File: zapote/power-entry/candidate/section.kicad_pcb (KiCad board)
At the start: 2 copper layers, 230 x 190 mm, 53 parts, among them U1 GBU2510A, U10 C3D20065D, U11 UCC28180D, U12 10mohm, U13 10ohm, U14 10kohm, U15 1kohm, U16 100kohm, U17 91ohm, U18 220ohm, U19 16.2kohm, U2 0031.2510, U20 200kohm, U21 200kohm, U22 200kohm, U23 200kohm, U24 200kohm, U25 13kohm, U26 40.2kohm, U27 1uF, U28 2.7nF, U29 4.7uF, U3 B82726S2163N030, U30 220nF, U31 1nF, U32 680pF, U33 AO3400A, U34 SS14, U35 BAT54H,115, U36 560uF, U37 560uF, U38 560uF, U39 560uF, U4 SL32 10015, U40 1nF, U41 1714984, U42 61300211121, U43 61300211121, U44 61300211121, U45 AO3400A, U46 AO3400A, U47 100kohm, U48 100kohm, U49 1kohm, U5 RT33K012, U50 100kohm, U51 1714971, U52 150kohm, U53 150kohm, U6 0.22uF, U7 V150LA10AP, U8 760800301, U9 STW65N65DM2

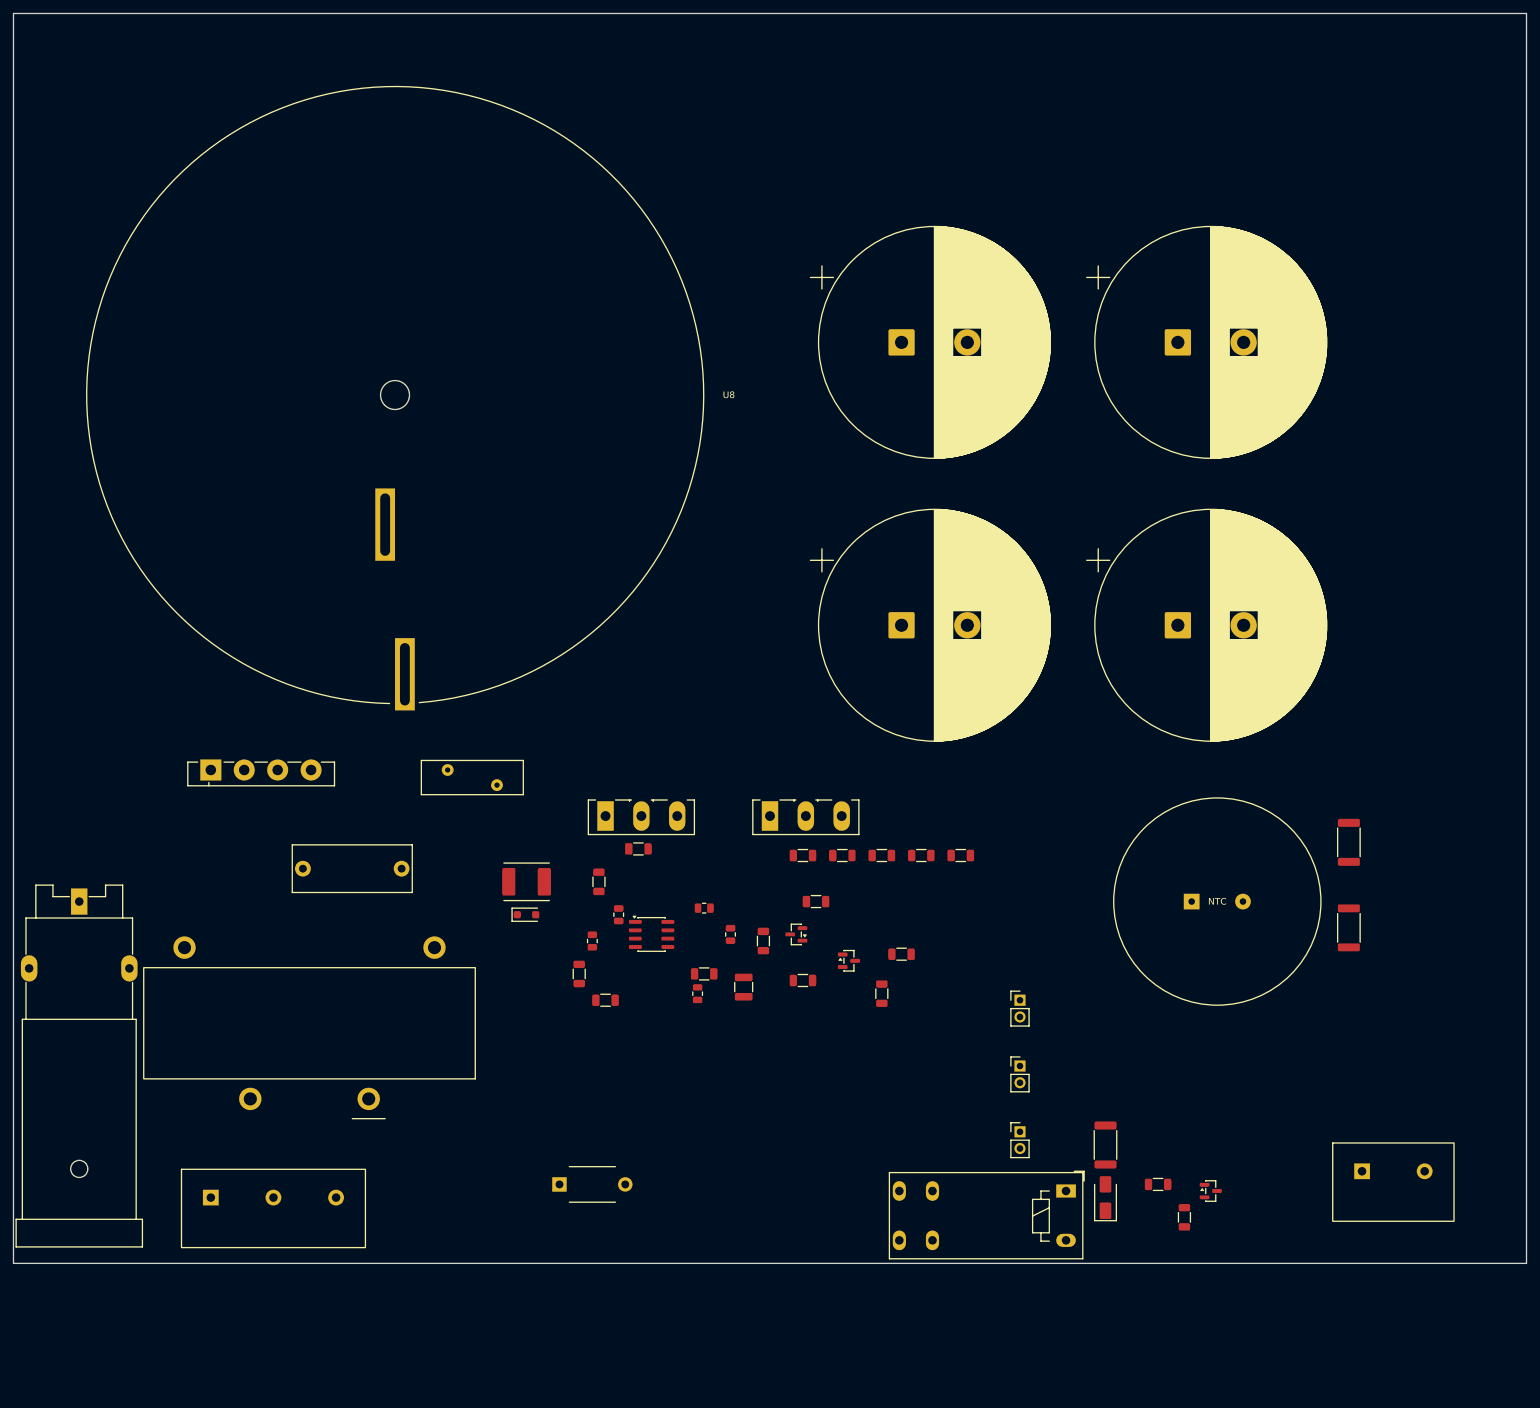
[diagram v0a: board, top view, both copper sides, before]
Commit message: fix(zapote): route PFC power entry and enforce voltage-domain clearances
Route the 54-part PFC candidate through explicit agent-authored paths and
validate saved copper against source connectivity and voltage-domain rules.
Retain native zero-violation ERC/DRC receipts, passing construction checks,
228 passing Rust tests, reviewed demo assets, and portable routing lessons.

Hardware qualification remains unrun; this is not a fabrication release.
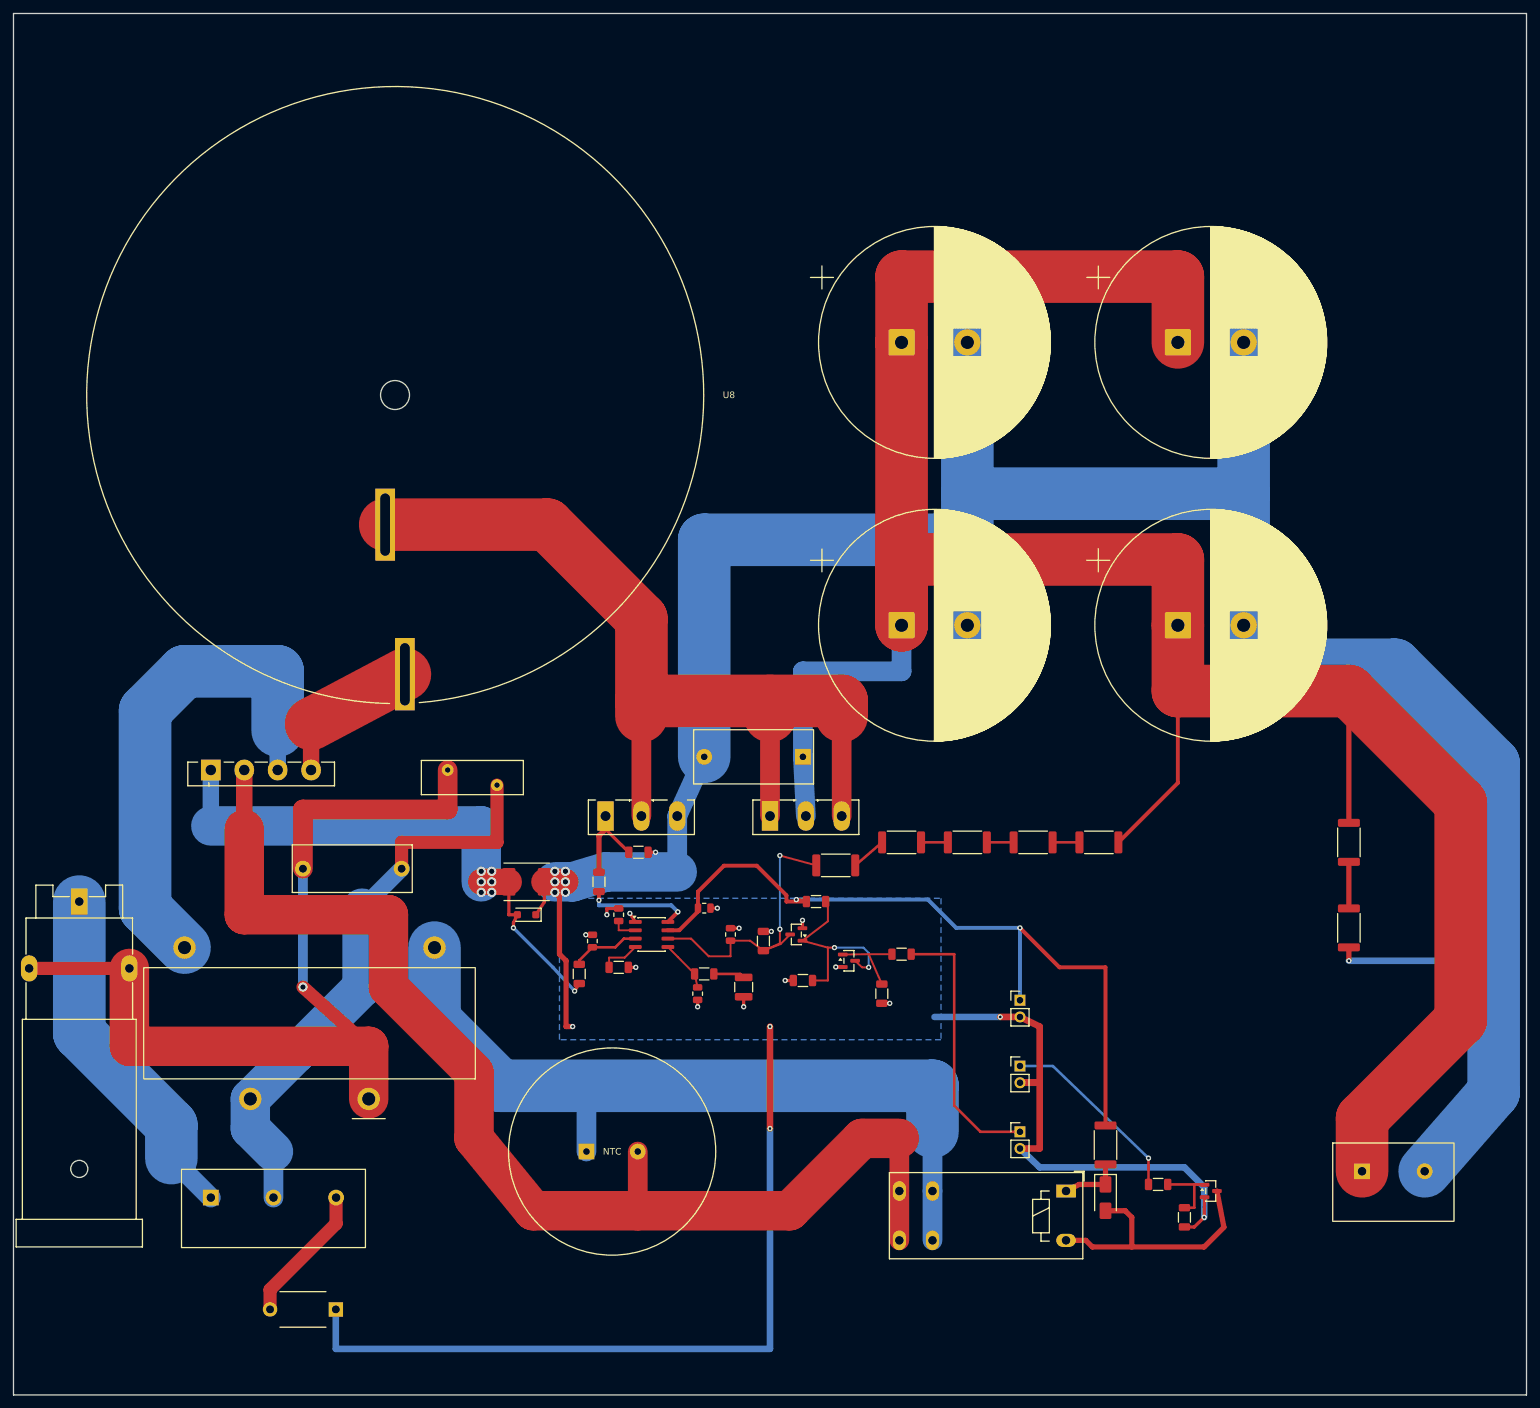
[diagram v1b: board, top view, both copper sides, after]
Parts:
- added U40: 470nF, temper:B32672P6474K000, F.Cu at (120.0, 113.0)
- U20, U21, U22, U23, U24: footprint Resistor_SMD:R_1206_3216Metric -> Resistor_SMD:R_2512_6332Metric
- moved U4 99.5 mm to (91.0, 173.0)
- moved U41 38.9 mm to (49.0, 197.0), turned to 180 degrees
- moved U20 21.1 mm to (165.0, 126.0)
- moved U21 17.1 mm to (155.0, 126.0)
- moved U22 13.2 mm to (145.0, 126.0)
- moved U23 9.22 mm to (135.0, 126.0)
- moved U19 5.39 mm to (92.0, 145.0)
- moved U24 5.22 mm to (125.0, 129.5)
- moved U14 0.50 mm to (95.0, 127.5)
- turned U12 to 180 degrees
- turned U16 to -90 degrees
- turned U17 to -90 degrees
- turned U18 to -90 degrees
- turned U29 to -90 degrees
- turned U30 to -90 degrees
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- renumbered U40 to U41, U41 to U42, U42 to U43, U43 to U44, U44 to U45, U45 to U46, U46 to U47, U47 to U48, U48 to U49, U49 to U50, U50 to U51, U51 to U52, U52 to U53, U53 to U54
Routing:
- net PFC_BUS_MINUS: track 0.00 -> 632.7 mm, vias 0 -> 26
- net PFC_BUS_PLUS_390V: track 0.00 -> 390.0 mm
- net ac1: track 0.00 -> 182.2 mm
- net a1: track 0.00 -> 140.3 mm
- net l1: track 0.00 -> 139.9 mm, vias 0 -> 1
- net l2: track 0.00 -> 124.3 mm
- net AUX_15V_IN: track 0.00 -> 117.6 mm, vias 0 -> 2
- net AC_N_RECTIFIED_INPUT: track 0.00 -> 88.2 mm
- net minus: track 0.00 -> 85.4 mm, vias 0 -> 8
- net ac2: track 0.00 -> 76.1 mm
- net AC_L_RECTIFIED_INPUT: track 0.00 -> 53.3 mm
- net vsense: track 0.00 -> 45.2 mm, vias 0 -> 2
- net HOT_PERMIT_EXTERNAL: track 0.00 -> 41.2 mm
- net coil2: track 0.00 -> 40.2 mm
- net q_inhibit-g: track 0.00 -> 30.7 mm, vias 0 -> 2
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- added copper zone on B.Cu, net PFC_BUS_MINUS
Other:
- board size 230 x 190 mm -> 230 x 210 mm
